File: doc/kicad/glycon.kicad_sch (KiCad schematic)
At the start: 53 parts, among them J1 Arduino/system bus header, J2 PMOD USBUART conn, J3 Conn_01x02, J4 Conn_02x24_Odd_Even, Q1 IRF9540N, Q2 IRF9540N, SW1 SW_Push, SW2 SW_Push, U0 Z80CPU, U1 628128_DIP32_SSOP32, U10 74HC244, U11 PIO-DIP-40, U12 CTC-DIP-28, U2 SST39SF010, U3 74HC32, U4 74HC04, U5 74LS21, U6 74LS139, U7 SIO0-DIP-40, U8 PIO-DIP-40, U9 74HC244, X1 ACO-6.144MHz

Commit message: add missing A8 pin to pinout diagram
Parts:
- added J?: USB_B, symbol Connector:USB_B
- added R? (x4): 10K, Resistor_THT:R_Axial_DIN0207_L6.3mm_D2.5mm_P10.16mm_Horizontal, symbol Device:R
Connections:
- net +5V: now also J?.1 (VBUS)
- net A2: now also R?.1
- net A3: now also R?.1
- net Earth: now also U6.1 (E), U6.15 (E), J?.4 (GND), J?.5 (Shield), R?.2, R?.2, R?.2, R?.2
- net PGA0: now also R?.1
- net PGA1: now also R?.1
- net VDD: no longer U6.1 (E), U6.15 (E)
- no-connect marks 5 -> 7
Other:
- moved on the sheet: U3A, U3B, U3C, U3D, U5A, U5B

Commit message: minor schematic updates
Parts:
- removed U5: 74LS21, Package_DIP:DIP-14_W7.62mm_Socket, symbol 74xx:74LS21
- added R? (x2): 10K, Resistor_THT:R_Axial_DIN0207_L6.3mm_D2.5mm_P10.16mm_Horizontal, symbol Device:R
- added U? (x4): 74LS08, symbol 74xx:74LS08
- gave numbers to parts that had none: 5
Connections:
- net ~{RD} is gone; now on net ~{IORD}: R2.1, U0.21 (~{RD}), U3.2
- net A14: now also J1.37 (Pin_37)
- net A15: now also J1.16 (Pin_16)
- net A16: now also J1.14 (Pin_14)
- net A17: now also J1.12 (Pin_12)
- net Earth: now also U1.22 (~{CS1}), U?.7 (GND); no longer U11.16 (~{ASTB}), U11.17 (~{BSTB}), U11.18 (ARDY), U11.21 (BRDY)
- net VDD: now also U0.24 (~{WAIT}), R?.1, R?.1, U?.14 (VCC); no longer U1.22 (~{CS1})
- net ~{INTIN}: now also U?.1
- net ~{INT}: now also U?.3
- net ~{M1}: now also U?.5, U?.9; no longer U11.37 (~{M1}), U8.37 (~{M1})
- net ~{RESET}: now also U?.10, U?.4
- net at U11.23 (~{INT}): now also U12.12 (~{INT}), U7.5 (~{INT}), U8.23 (~{INT}), R?.2, U?.2
- new net: U8.37 (~{M1}), U?.8
- new net: U11.37 (~{M1}), U?.6
- no-connect marks 7 -> 11
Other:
- moved on the sheet: R16, R7

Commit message: schematic fixes
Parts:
- U: renamed from H3; value MountingHole_Pad -> (none); footprint MountingHole:MountingHole_3.2mm_M3_Pad -> (none)
- U: renamed from R2; value 10K -> (none); footprint Resistor_THT:R_Axial_DIN0207_L6.3mm_D2.5mm_P10.16mm_Horizontal -> (none)
- U: renamed from C6; value 100nF -> (none); footprint Capacitor_THT:C_Disc_D4.7mm_W2.5mm_P5.00mm -> (none)
- U: renamed from SW1; value SW_Push -> (none); footprint Button_Switch_THT:SW_PUSH_6mm -> (none)
- U: renamed from U?; value 74LS08 -> (none)
- U: renamed from R9; value 10K -> (none); footprint Resistor_THT:R_Axial_DIN0207_L6.3mm_D2.5mm_P10.16mm_Horizontal -> (none)
- U: renamed from C13; value 100nF -> (none); footprint Capacitor_THT:C_Disc_D4.7mm_W2.5mm_P5.00mm -> (none)
- U: renamed from J3; value Conn_01x02 -> (none); footprint Connector_PinHeader_2.54mm:PinHeader_1x02_P2.54mm_Vertical -> (none)
- U: renamed from U3; value 74HC32 -> (none); footprint Package_DIP:DIP-14_W7.62mm_Socket -> (none)
- U: renamed from U4; value 74HC04 -> (none); footprint Package_DIP:DIP-14_W7.62mm_Socket -> (none)
- U: renamed from X1; value ACO-6.144MHz -> (none); footprint Oscillator:Oscillator_DIP-14 -> (none)
- U: renamed from U11; value PIO-DIP-40 -> (none); footprint Package_DIP:DIP-40_W15.24mm_Socket -> (none)
- U: renamed from J4; value Conn_02x24_Odd_Even -> (none); footprint Connector_PinSocket_2.54mm:PinSocket_2x24_P2.54mm_Vertical -> (none)
- U: renamed from R11; value 10K -> (none); footprint Resistor_THT:R_Axial_DIN0207_L6.3mm_D2.5mm_P10.16mm_Horizontal -> (none)
- U: renamed from R15; value 10K -> (none); footprint Resistor_THT:R_Axial_DIN0207_L6.3mm_D2.5mm_P10.16mm_Horizontal -> (none)
- U: renamed from C5; value 100nF -> (none); footprint Capacitor_THT:C_Disc_D4.7mm_W2.5mm_P5.00mm -> (none)
- U: renamed from C8; value 100nF -> (none); footprint Capacitor_THT:C_Disc_D4.7mm_W2.5mm_P5.00mm -> (none)
- U: renamed from H1; value MountingHole_Pad -> (none); footprint MountingHole:MountingHole_3.2mm_M3_Pad -> (none)
- U: renamed from J1; value Arduino/system bus header -> (none); footprint Connector_PinSocket_2.54mm:PinSocket_2x20_P2.54mm_Vertical -> (none)
- U: renamed from Q2; value IRF9540N -> (none); footprint Package_TO_SOT_THT:TO-220-3_Vertical -> (none)
- U: renamed from R7; value 10K -> (none); footprint Resistor_THT:R_Axial_DIN0207_L6.3mm_D2.5mm_P10.16mm_Horizontal -> (none)
- U: renamed from U7; value SIO0-DIP-40 -> (none); footprint Package_DIP:DIP-40_W15.24mm_Socket -> (none)
- U: renamed from J2; value PMOD USBUART conn -> (none); footprint Connector_PinHeader_2.54mm:PinHeader_1x06_P2.54mm_Vertical -> (none)
- U: renamed from C10; value 100nF -> (none); footprint Capacitor_THT:C_Disc_D4.7mm_W2.5mm_P5.00mm -> (none)
- U: renamed from R14; value 10K -> (none); footprint Resistor_THT:R_Axial_DIN0207_L6.3mm_D2.5mm_P10.16mm_Horizontal -> (none)
- U: renamed from R3; value 10K -> (none); footprint Resistor_THT:R_Axial_DIN0207_L6.3mm_D2.5mm_P10.16mm_Horizontal -> (none)
- U: renamed from H4; value MountingHole_Pad -> (none); footprint MountingHole:MountingHole_3.2mm_M3_Pad -> (none)
- U: renamed from C3; value 100nF -> (none); footprint Capacitor_THT:C_Disc_D4.7mm_W2.5mm_P5.00mm -> (none)
- U: renamed from Q1; value IRF9540N -> (none); footprint Package_TO_SOT_THT:TO-220-3_Vertical -> (none)
- U: renamed from R10; value 10K -> (none); footprint Resistor_THT:R_Axial_DIN0207_L6.3mm_D2.5mm_P10.16mm_Horizontal -> (none)
- U: renamed from R16; value 10K -> (none); footprint Resistor_THT:R_Axial_DIN0207_L6.3mm_D2.5mm_P10.16mm_Horizontal -> (none)
- U: renamed from C1; value 100nF -> (none); footprint Capacitor_THT:C_Disc_D4.7mm_W2.5mm_P5.00mm -> (none)
- U: renamed from C2; value 100nF -> (none); footprint Capacitor_THT:C_Disc_D4.7mm_W2.5mm_P5.00mm -> (none)
- U: renamed from U0; value Z80CPU -> (none); footprint Package_DIP:DIP-40_W15.24mm_Socket -> (none)
- U: renamed from U6; value 74LS139 -> (none); footprint Package_DIP:DIP-16_W7.62mm_Socket -> (none)
- U: renamed from J5; value USB_B -> (none)
- U: renamed from U1; value 628128_DIP32_SSOP32 -> (none); footprint Package_DIP:DIP-32_W15.24mm_Socket -> (none)
- U: renamed from H2; value MountingHole_Pad -> (none); footprint MountingHole:MountingHole_3.2mm_M3_Pad -> (none)
- U: renamed from U2; value SST39SF010 -> (none); footprint Package_DIP:DIP-32_W15.24mm_Socket -> (none)
- U: renamed from R1; value 10K -> (none); footprint Resistor_THT:R_Axial_DIN0207_L6.3mm_D2.5mm_P10.16mm_Horizontal -> (none)
- U: renamed from R?; value 10K -> (none); footprint Resistor_THT:R_Axial_DIN0207_L6.3mm_D2.5mm_P10.16mm_Horizontal -> (none)
- U: renamed from C11; value 100nF -> (none); footprint Capacitor_THT:C_Disc_D4.7mm_W2.5mm_P5.00mm -> (none)
- U: renamed from H5; value MountingHole_Pad -> (none); footprint MountingHole:MountingHole_3.2mm_M3_Pad -> (none)
- U: renamed from U8; value PIO-DIP-40 -> (none); footprint Package_DIP:DIP-40_W15.24mm_Socket -> (none)
- U: renamed from SW2; value SW_Push -> (none); footprint Button_Switch_THT:SW_PUSH_6mm -> (none)
- U: renamed from U9; value 74HC244 -> (none); footprint Package_DIP:DIP-20_W7.62mm_Socket -> (none)
- U: renamed from C4; value 100nF -> (none); footprint Capacitor_THT:C_Disc_D4.7mm_W2.5mm_P5.00mm -> (none)
- U: renamed from R12; value 470 -> (none); footprint Resistor_THT:R_Axial_DIN0207_L6.3mm_D2.5mm_P10.16mm_Horizontal -> (none)
- U: renamed from U10; value 74HC244 -> (none); footprint Package_DIP:DIP-20_W7.62mm_Socket -> (none)
- U: renamed from R6; value 10K -> (none); footprint Resistor_THT:R_Axial_DIN0207_L6.3mm_D2.5mm_P10.16mm_Horizontal -> (none)
- U: renamed from C7; value 100nF -> (none); footprint Capacitor_THT:C_Disc_D4.7mm_W2.5mm_P5.00mm -> (none)
- U: renamed from R13; value 10K -> (none); footprint Resistor_THT:R_Axial_DIN0207_L6.3mm_D2.5mm_P10.16mm_Horizontal -> (none)
- U: renamed from C9; value 100nF -> (none); footprint Capacitor_THT:C_Disc_D4.7mm_W2.5mm_P5.00mm -> (none)
- U: renamed from U12; value CTC-DIP-28 -> (none); footprint Package_DIP:DIP-28_W15.24mm_Socket -> (none)
- U: renamed from C12; value 100nF -> (none); footprint Capacitor_THT:C_Disc_D4.7mm_W2.5mm_P5.00mm -> (none)
- U: renamed from R4; value 10K -> (none); footprint Resistor_THT:R_Axial_DIN0207_L6.3mm_D2.5mm_P10.16mm_Horizontal -> (none)
- U: renamed from R8; value 10K -> (none); footprint Resistor_THT:R_Axial_DIN0207_L6.3mm_D2.5mm_P10.16mm_Horizontal -> (none)
- U: renamed from R5; value 10K -> (none); footprint Resistor_THT:R_Axial_DIN0207_L6.3mm_D2.5mm_P10.16mm_Horizontal -> (none)
- U: renamed from D1; value LED -> (none); footprint LED_THT:LED_D5.0mm -> (none)
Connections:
- net A2: now also U.2 (A0); no longer U.14 (A0)
- net A3: now also U.3 (A1); no longer U.13 (A1)
- net BUSRQ: now also U.1; no longer U.3
- net Earth: now also U.1 (E); no longer U.15 (E), U.7 (GND), U.7 (GND), U.7 (GND), U.8 (GND)
- net RAM WE: now also U.1; no longer U.9
- net RAM/ROM OE: now also U.1; no longer U.4
- net RESET: now also U.1; no longer U.5
- net VDD: no longer U.14 (VCC), U.14 (VCC), U.14 (VCC), U.16 (VCC)
- net ~{M1}: now also U.1, U.2; no longer U.5, U.9
- net ~{MEMRD}: now also U.3; no longer U.6
- net ~{RESET}: now also U.1, U.2, U.2; no longer U.10, U.4, U.6
- net at U.37 (~{M1}): now also U.3; no longer U.8
- net at U.1, U.1, U.19 (~{MREQ}): now also U.1; no longer U.12
- net at U.1, U.22 (~{WR}): now also U.2; no longer U.13
- net at U.37 (~{M1}): now also U.3; no longer U.6
- net at U.4 (~{CE}): now also U.4 (O0); no longer U.12 (O0)
- net at U.3: now also U.2; no longer U.5
- net at U.25 (~{BUSRQ}): now also U.2; no longer U.4
- net at U.35 (~{CE}): now also U.7 (O3); no longer U.9 (O3)
- net at U.29 (~{WE}): now also U.3; no longer U.8
- net at U.4 (~{CE}): now also U.6 (O2); no longer U.10 (O2)
- net at U.16 (~{CE}): now also U.5 (O1); no longer U.11 (O1)
- new net: U.2, U.3

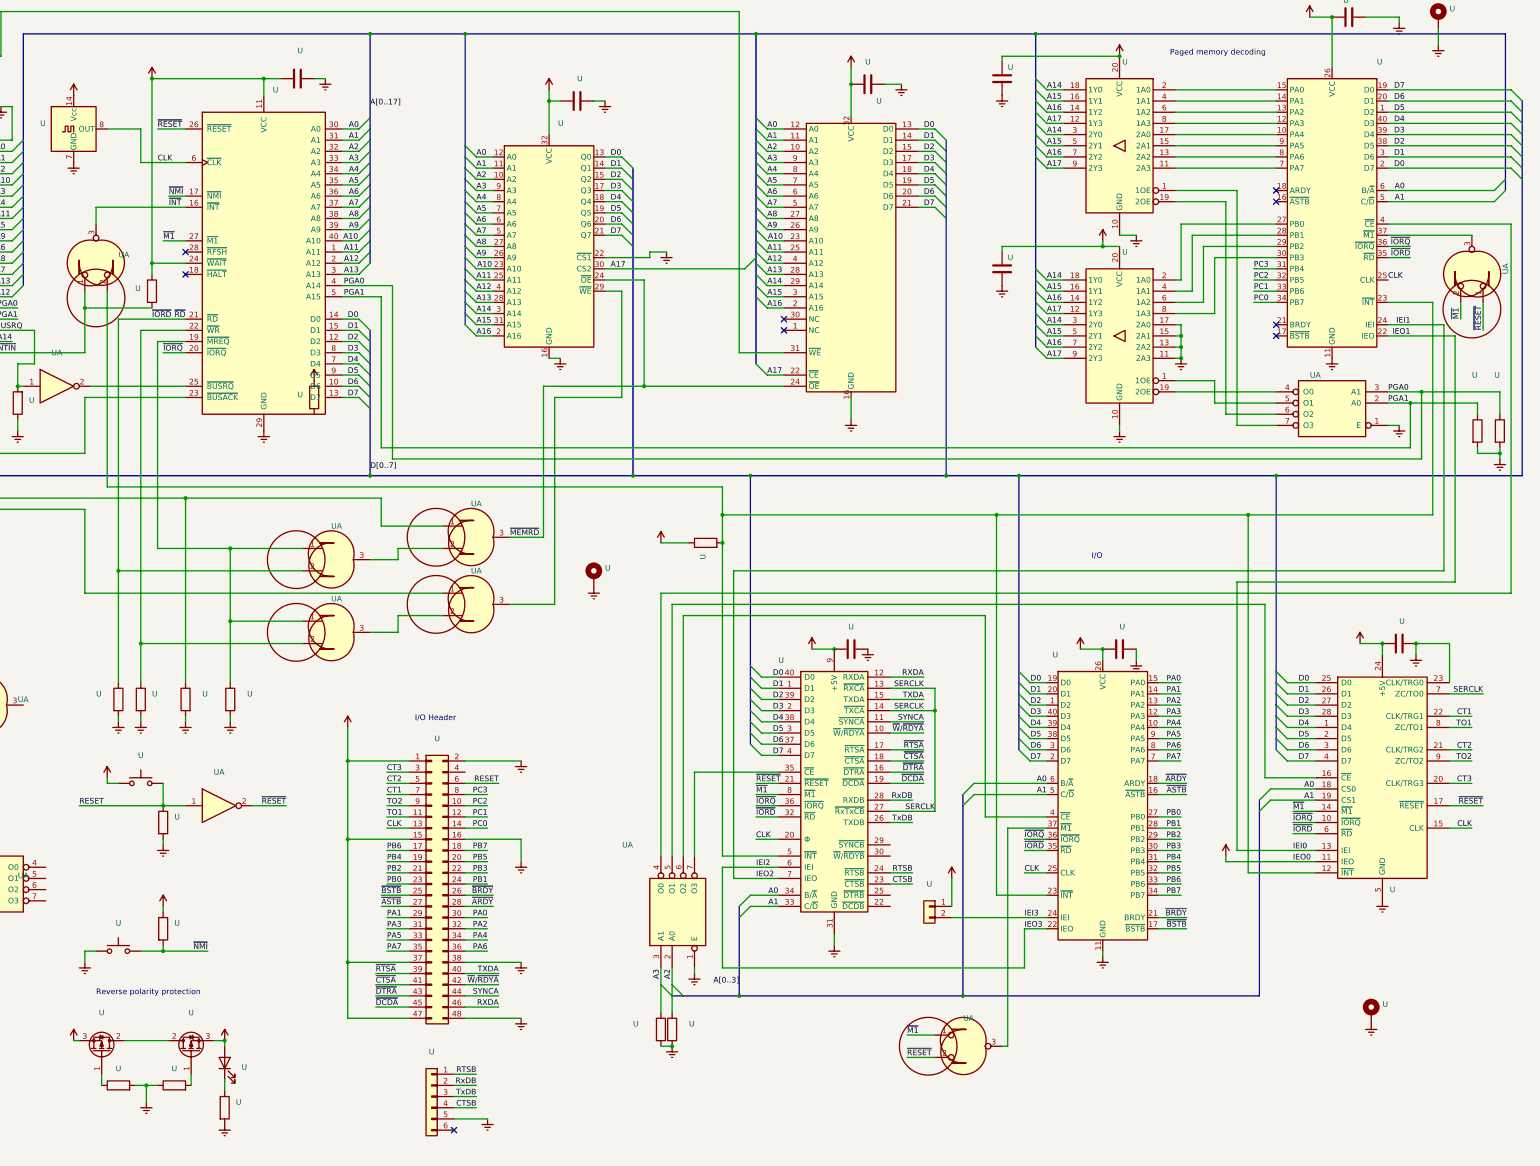
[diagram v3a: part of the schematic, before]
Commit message: More schematic fixes
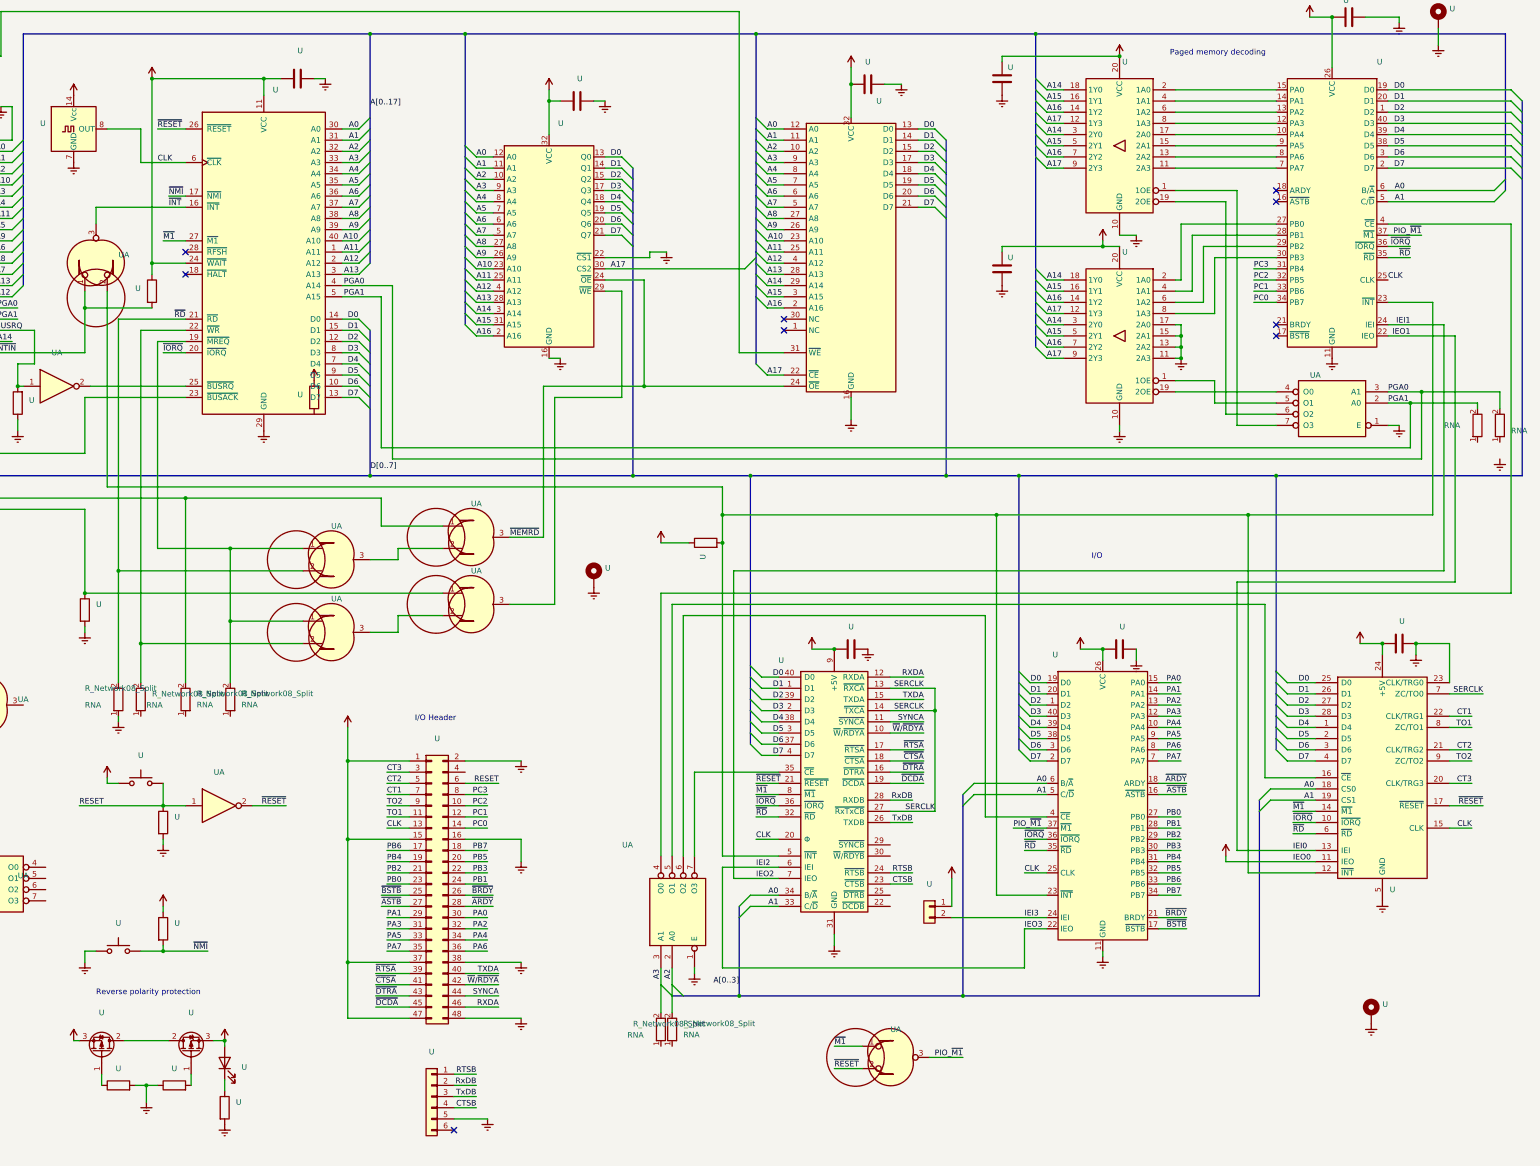
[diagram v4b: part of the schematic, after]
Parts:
- removed U (x8): (no value), symbol Device:R
- removed U: (no value), symbol 74xx:74LS08
- added RN (x8): R_Network08_Split, Resistor_THT:R_Array_SIP9, symbol Device:R_Network08_Split
- added U: (no value), symbol Device:R
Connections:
- net A2: now also RN.2 (R1.2)
- net A3: now also RN.2 (R1.2)
- net D0: now also U.19 (D0); no longer U.2 (D7)
- net D1: now also U.20 (D1); no longer U.3 (D6)
- net D2: now also U.1 (D2); no longer U.38 (D5)
- net D3: now also U.40 (D3); no longer U.39 (D4)
- net D4: now also U.39 (D4); no longer U.40 (D3)
- net D5: now also U.38 (D5); no longer U.1 (D2)
- net D6: now also U.3 (D6); no longer U.20 (D1)
- net D7: now also U.2 (D7); no longer U.19 (D0)
- net Earth: now also RN.1 (R1.1), U.2
- net PGA0: now also RN.2 (R1.2)
- net PGA1: now also RN.2 (R1.2)
- net RAM WE: now also U.1
- net RAM/ROM OE: now also RN.2 (R1.2)
- net PIO_~{M1}: now reaches U.3, U.37 (~{M1})
- net PIO_~{M1}: now also U.37 (~{M1})
- net at U.1, U.1, U.19 (~{MREQ}): now also RN.2 (R1.2)
- net at U.2, U.22 (~{WR}): now also RN.2 (R1.2)
- net ~{IORD} renamed ~{RD}
- net ~{RD}: now also RN.2 (R1.2)
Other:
- moved on the sheet: UA
